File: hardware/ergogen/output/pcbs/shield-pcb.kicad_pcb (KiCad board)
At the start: 2 copper layers, 115 x 93.8 mm, 24 parts

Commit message: new 3d chain
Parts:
- added MH4: , ceoloide:mounting_hole_npth, F.Cu at (234.9, 154.7)
- moved MH3 41.4 mm to (232.0, 113.4), turned to 0 degrees
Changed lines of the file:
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@@
   (title_block
     (title "shield-pcb")
-    (date "2026-07-25")
+    (date "2026-08-05")
     (rev "1.2")
     (company "imochoa")
@@
   (footprint "ceoloide:mounting_hole_npth"
     (layer "F.Cu")
+    (at 232 113.35749999999999 0)
+    (property "Reference" "MH3"
+      (at 0 2.55 0)
+      (layer "F.SilkS")
+      hide
+      (effects (font (size 1 1) (thickness 0.15)))
+    )
+    (pad "" np_thru_hole circle
+      (at 0 0 0)
+      (size 2.2 2.2)
+      (drill 2.2)
+      (layers "*.Cu" "*.Mask")
+    )
+  )
+  (footprint "ceoloide:mounting_hole_npth"
+    (layer "F.Cu")
     (at 234.93715810000003 154.66270425 -22.5)
-    (property "Reference" "MH3"
+    (property "Reference" "MH4"
       (at 0 2.55 -22.5)
       (layer "F.SilkS")

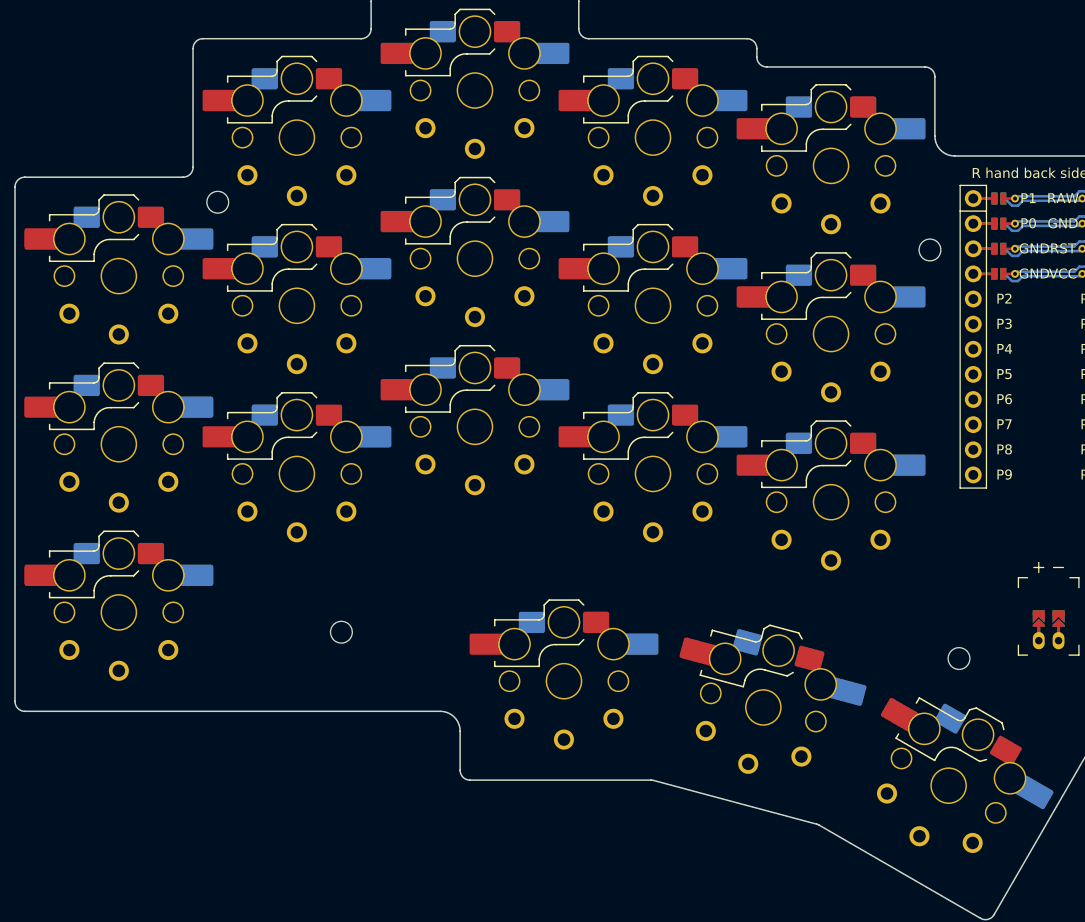
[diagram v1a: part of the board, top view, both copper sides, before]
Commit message: feat: add LED key matrix revision
Replace direct-pin scanning with a reversible 5x4 diode matrix and add an 18-key SK6812 chain to each half.

Configure ZMK matrix scanning, split transforms, SPI underglow, conservative brightness defaults, and RGB key controls. Regenerate the PCB and document the wiring and battery-pin changes.
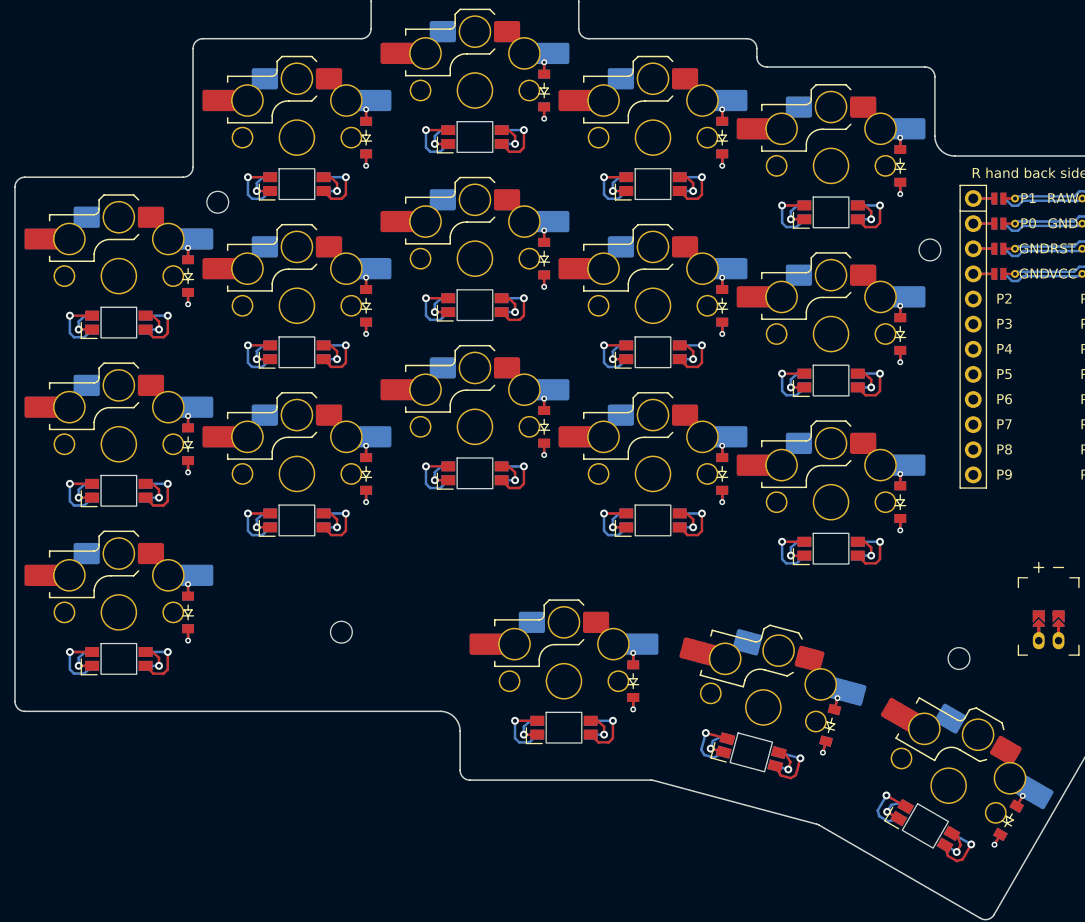
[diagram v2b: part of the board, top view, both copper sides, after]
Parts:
- added D1: , ceoloide:diode_tht_sod123, F.Cu at (157.0, 150.0)
- added D10: , ceoloide:diode_tht_sod123, F.Cu at (211.0, 136.0)
- added D11: , ceoloide:diode_tht_sod123, F.Cu at (211.0, 119.0)
- added D12: , ceoloide:diode_tht_sod123, F.Cu at (211.0, 102.0)
- added D13: , ceoloide:diode_tht_sod123, F.Cu at (229.0, 138.9)
- added D14: , ceoloide:diode_tht_sod123, F.Cu at (229.0, 121.9)
- added D15: , ceoloide:diode_tht_sod123, F.Cu at (229.0, 104.9)
- added D16: , ceoloide:diode_tht_sod123, F.Cu at (202.0, 157.0)
- added D17: , ceoloide:diode_tht_sod123, F.Cu at (221.9, 161.4)
- added D18: , ceoloide:diode_tht_sod123, F.Cu at (239.9, 171.0)
- added D2: , ceoloide:diode_tht_sod123, F.Cu at (157.0, 133.0)
- added D3: , ceoloide:diode_tht_sod123, F.Cu at (157.0, 116.0)
- added D4: , ceoloide:diode_tht_sod123, F.Cu at (175.0, 136.0)
- added D5: , ceoloide:diode_tht_sod123, F.Cu at (175.0, 119.0)
- added D6: , ceoloide:diode_tht_sod123, F.Cu at (175.0, 102.0)
- added D7: , ceoloide:diode_tht_sod123, F.Cu at (193.0, 131.2)
- added D8: , ceoloide:diode_tht_sod123, F.Cu at (193.0, 114.2)
- added D9: , ceoloide:diode_tht_sod123, F.Cu at (193.0, 97.2)
- added LED1: , ceoloide:led_SK6812mini-e (per-key, reversible), B.Cu at (150.0, 154.7)
- added LED10: , ceoloide:led_SK6812mini-e (per-key, reversible), B.Cu at (204.0, 140.7)
- added LED11: , ceoloide:led_SK6812mini-e (per-key, reversible), B.Cu at (204.0, 123.7)
- added LED12: , ceoloide:led_SK6812mini-e (per-key, reversible), B.Cu at (204.0, 106.7)
- added LED13: , ceoloide:led_SK6812mini-e (per-key, reversible), B.Cu at (222.0, 143.6)
- added LED14: , ceoloide:led_SK6812mini-e (per-key, reversible), B.Cu at (222.0, 126.6)
- added LED15: , ceoloide:led_SK6812mini-e (per-key, reversible), B.Cu at (222.0, 109.6)
- added LED16: , ceoloide:led_SK6812mini-e (per-key, reversible), B.Cu at (195.0, 161.7)
- added LED17: , ceoloide:led_SK6812mini-e (per-key, reversible), B.Cu at (213.9, 164.1)
- added LED18: , ceoloide:led_SK6812mini-e (per-key, reversible), B.Cu at (231.5, 171.6)
- added LED2: , ceoloide:led_SK6812mini-e (per-key, reversible), B.Cu at (150.0, 137.7)
- added LED3: , ceoloide:led_SK6812mini-e (per-key, reversible), B.Cu at (150.0, 120.7)
- added LED4: , ceoloide:led_SK6812mini-e (per-key, reversible), B.Cu at (168.0, 140.7)
- added LED5: , ceoloide:led_SK6812mini-e (per-key, reversible), B.Cu at (168.0, 123.7)
- added LED6: , ceoloide:led_SK6812mini-e (per-key, reversible), B.Cu at (168.0, 106.7)
- added LED7: , ceoloide:led_SK6812mini-e (per-key, reversible), B.Cu at (186.0, 135.9)
- added LED8: , ceoloide:led_SK6812mini-e (per-key, reversible), B.Cu at (186.0, 118.9)
- added LED9: , ceoloide:led_SK6812mini-e (per-key, reversible), B.Cu at (186.0, 101.9)
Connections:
- MCU1 pad 10: thumb-zn_near_thumb -> col3
- MCU1 pad 11: thumb-zn_home_thumb -> LED_DATA
- MCU1 pad 12: thumb-zn_far_thumb -> P10
- MCU1 pad 123: grid-zn_ring_top -> P0
- MCU1 pad 124: grid-zn_middle_top -> P1
- MCU1 pad 13: grid-zn_inner_bottom -> P9
- MCU1 pad 14: grid-zn_index_bottom -> P8
- MCU1 pad 15: grid-zn_middle_bottom -> row3
- MCU1 pad 16: grid-zn_ring_bottom -> row2
- MCU1 pad 17: grid-zn_ring_home -> row1
- MCU1 pad 18: grid-zn_inner_home -> row0
- MCU1 pad 19: grid-zn_index_home -> P3
- MCU1 pad 20: grid-zn_middle_home -> P2
- MCU1 pad 5: grid-zn_inner_top -> P21
- MCU1 pad 6: grid-zn_index_top -> col2
- MCU1 pad 7: grid-zn_pinky_top -> col1
- MCU1 pad 8: grid-zn_pinky_home -> col0
- MCU1 pad 9: grid-zn_pinky_bottom -> col4
- S1 pad 1: grid-zn_pinky_bottom -> col0
- S1 pad 2: GND -> grid-zn_pinky_bottom
- S10 pad 1: grid-zn_index_bottom -> col3
- S10 pad 2: GND -> grid-zn_index_bottom
- S11 pad 1: grid-zn_index_home -> col3
- S11 pad 2: GND -> grid-zn_index_home
- S12 pad 1: grid-zn_index_top -> col3
- S12 pad 2: GND -> grid-zn_index_top
- S13 pad 1: grid-zn_inner_bottom -> col4
- S13 pad 2: GND -> grid-zn_inner_bottom
- S14 pad 1: grid-zn_inner_home -> col4
- S14 pad 2: GND -> grid-zn_inner_home
- S15 pad 1: grid-zn_inner_top -> col4
- S15 pad 2: GND -> grid-zn_inner_top
- S16 pad 1: thumb-zn_near_thumb -> col2
- S16 pad 2: GND -> thumb-zn_near_thumb
- S17 pad 1: thumb-zn_home_thumb -> col3
- S17 pad 2: GND -> thumb-zn_home_thumb
- S18 pad 1: thumb-zn_far_thumb -> col4
- S18 pad 2: GND -> thumb-zn_far_thumb
- S2 pad 1: grid-zn_pinky_home -> col0
- S2 pad 2: GND -> grid-zn_pinky_home
- S3 pad 1: grid-zn_pinky_top -> col0
- S3 pad 2: GND -> grid-zn_pinky_top
- S4 pad 1: grid-zn_ring_bottom -> col1
- S4 pad 2: GND -> grid-zn_ring_bottom
- S5 pad 1: grid-zn_ring_home -> col1
- S5 pad 2: GND -> grid-zn_ring_home
- S6 pad 1: grid-zn_ring_top -> col1
- S6 pad 2: GND -> grid-zn_ring_top
- S7 pad 1: grid-zn_middle_bottom -> col2
- S7 pad 2: GND -> grid-zn_middle_bottom
- S8 pad 1: grid-zn_middle_home -> col2
- S8 pad 2: GND -> grid-zn_middle_home
- S9 pad 1: grid-zn_middle_top -> col2
- S9 pad 2: GND -> grid-zn_middle_top
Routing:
- net GND: track 0.00 -> 67.6 mm, vias 0 -> 18
- net VCC: track 0.00 -> 67.6 mm, vias 0 -> 18
- net led_17: track 0.00 -> 13.5 mm, vias 0 -> 2
- net led_16: track 0.00 -> 13.5 mm, vias 0 -> 2
- net led_15: track 0.00 -> 13.5 mm, vias 0 -> 2
- net led_11: track 0.00 -> 13.5 mm, vias 0 -> 2
- net led_6: track 0.00 -> 13.5 mm, vias 0 -> 2
- net led_5: track 0.00 -> 13.5 mm, vias 0 -> 2
- net led_10: track 0.00 -> 13.5 mm, vias 0 -> 2
- net led_9: track 0.00 -> 13.5 mm, vias 0 -> 2
- net led_8: track 0.00 -> 13.5 mm, vias 0 -> 2
- net led_7: track 0.00 -> 13.5 mm, vias 0 -> 2
- net led_4: track 0.00 -> 13.5 mm, vias 0 -> 2
- net led_3: track 0.00 -> 13.5 mm, vias 0 -> 2
- net led_2: track 0.00 -> 13.5 mm, vias 0 -> 2
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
